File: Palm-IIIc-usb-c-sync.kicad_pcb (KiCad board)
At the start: 4 copper layers, 26 x 10 mm, 28 parts, among them J1 USB_C_Receptacle_USB2.0, J2 Conn_01x05, J3 Conn_01x05, U1 CP2102N-Axx-xQFN20, U2 TRSF3232E

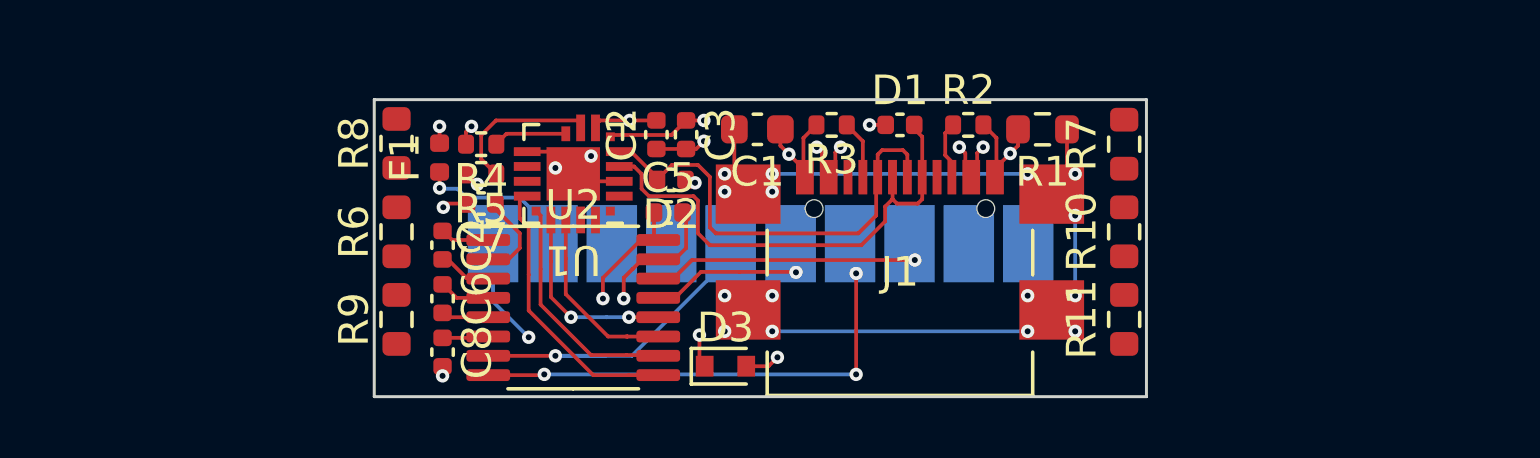
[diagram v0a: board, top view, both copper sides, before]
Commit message: Add manufacturing markings
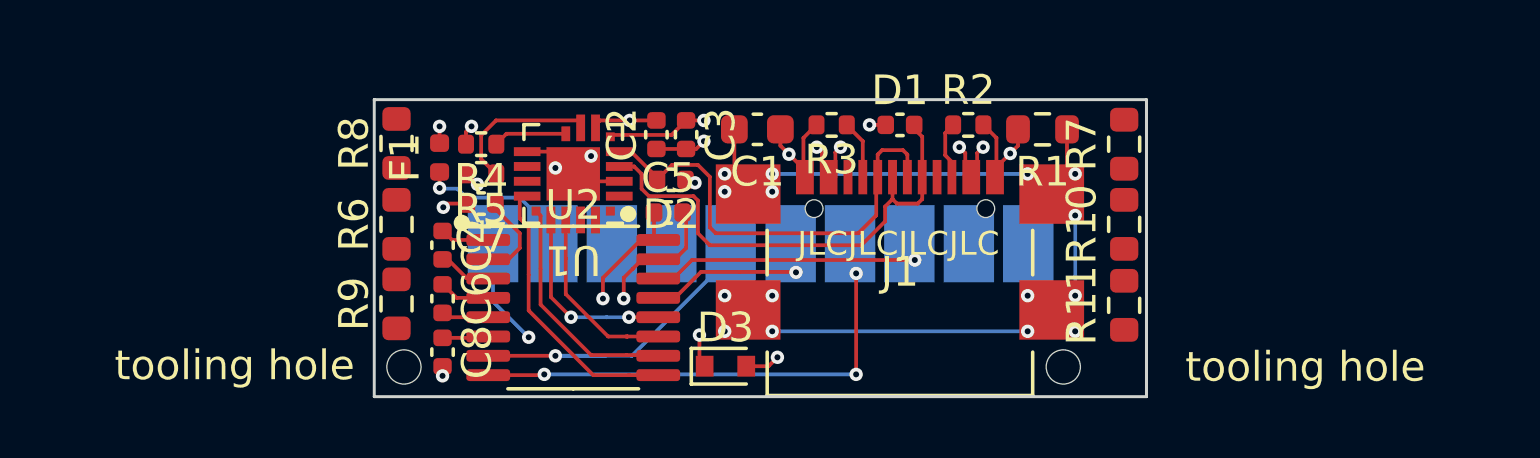
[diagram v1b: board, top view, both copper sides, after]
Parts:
- added H1: MountingHole, ToolingHole:ToolingHole_JLCSMT, F.Cu at (73.2, 59.0)
- added H2: MountingHole, ToolingHole:ToolingHole_JLCSMT, F.Cu at (51.0, 59.0)
- moved R9 0.52 mm to (50.8, 56.9)
- moved R11 0.48 mm to (75.2, 56.9)
- moved R10 0.25 mm to (75.2, 54.2)
- moved R6 0.25 mm to (50.8, 54.2)
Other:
- board text added: "JLCJLCJLCJLC"
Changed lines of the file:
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@@
 (kicad_pcb (version 20211014) (generator pcbnew)
   (general
-    (thickness 4.69)
+    (thickness 1.999999)
   )
   (paper "A4")
@@
       (layer "F.Mask" (type "Top Solder Mask") (thickness 0.01))
       (layer "F.Cu" (type "copper") (thickness 0.035))
-      (layer "dielectric 1" (type "core") (thickness 1.51) (material "FR4") (epsilon_r 4.5) (loss_tangent 0.02))
+      (layer "dielectric 1" (type "core") (thickness 0.613333) (material "FR4") (epsilon_r 4.5) (loss_tangent 0.02))
       (layer "In1.Cu" (type "copper") (thickness 0.035))
-      (layer "dielectric 2" (type "prepreg") (thickness 1.51) (material "FR4") (epsilon_r 4.5) (loss_tangent 0.02))
+      (layer "dielectric 2" (type "prepreg") (thickness 0.613333) (material "FR4") (epsilon_r 4.5) (loss_tangent 0.02))
       (layer "In2.Cu" (type "copper") (thickness 0.035))
-      (layer "dielectric 3" (type "core") (thickness 1.51) (material "FR4") (epsilon_r 4.5) (loss_tangent 0.02))
+      (layer "dielectric 3" (type "core") (thickness 0.613333) (material "FR4") (epsilon_r 4.5) (loss_tangent 0.02))
       (layer "B.Cu" (type "copper") (thickness 0.035))
       (layer "B.Mask" (type "Bottom Solder Mask") (thickness 0.01))
@@
   (net 48 "unconnected-(R11-Pad1)")
   (net 49 "unconnected-(R11-Pad2)")
+  (footprint "ToolingHole:ToolingHole_JLCSMT" (layer "F.Cu")
+    (at 51 59)
+    (property "Sheetfile" "Palm-IIIc-usb-c-sync.kicad_sch")
+    (property "Sheetname" "")
+    (property "exclude_from_bom" "")
+    (attr through_hole exclude_from_bom)
+    (fp_text reference "H2" (at 0 0.5) (layer "F.SilkS") hide
+      (effects (font (size 1 1) (thickness 0.15)))
+    )
+    (fp_text value "MountingHole" (at 0 -0.5) (layer "F.Fab")
+      (effects (font (size 1 1) (thickness 0.15)))
+    )
+    (fp_text user "tooling hole" (at -5.7 -0.05) (layer "F.SilkS")
+      (effects (font (size 1 1) (thickness 0.15)))
+    )
+    (pad "" np_thru_hole circle locked (at 0 0) (size 1.152 1.152) (drill 1.152) (layers *.Cu *.Mask))
+  )
   (footprint "Diode_SMD:D_SOD-523" (layer "F.Cu")
     (at 61.825 58.975)
@@
   )
   (footprint "Resistor_SMD:R_0603_1608Metric" (layer "F.Cu")
-    (at 50.75 57.4 90)
+    (at 50.75 56.875 90)
     (descr "Resistor SMD 0603 (1608 Metric), square (rectangular) end terminal, IPC_7351 nominal, (Body size source: IPC-SM-782 page 72, https://www.pcb-3d.com/wordpress/wp-content/uploads/ipc-sm-782a_amendment_1_and_2.pdf), generated with kicad-footprint-generator")
     (tags "resistor")
@@
   (footprint "Package_DFN_QFN_SiLabs:SilivonLabs_QFN-20-1EP_3x3mm_P0.5mm_missing_pads" (layer "F.Cu")
     (at 56.7 52.5 180)
+    (property "LCSC" "C969913")
     (property "Sheetfile" "Palm-IIIc-usb-c-sync.kicad_sch")
     (property "Sheetname" "")
@@
     )
   )
+  (footprint "ToolingHole:ToolingHole_JLCSMT" (layer "F.Cu")
+    (at 73.2 59)
+    (property "Sheetfile" "Palm-IIIc-usb-c-sync.kicad_sch")
+    (property "Sheetname" "")
+    (property "exclude_from_bom" "")
+    (attr through_hole exclude_from_bom)
+    (fp_text reference "H1" (at 0 0.5) (layer "F.SilkS") hide
+      (effects (font (size 1 1) (thickness 0.15)))
+    )
+    (fp_text value "MountingHole" (at 0 -0.5) (layer "F.Fab")
+      (effects (font (size 1 1) (thickness 0.15)))
+    )
+    (fp_text user "tooling hole" (at 8.15 0) (layer "F.SilkS")
+      (effects (font (size 1 1) (thickness 0.15)))
+    )
+    (pad "" np_thru_hole circle locked (at 0 0) (size 1.152 1.152) (drill 1.152) (layers *.Cu *.Mask))
+  )
   (footprint "Capacitor_SMD:C_0402_1005Metric" (layer "F.Cu")
     (at 67.7 50.85)
@@
     (descr "TSSOP, 16 Pin (JEDEC MO-153 Var AB https://www.jedec.org/document_search?search_api_views_fulltext=MO-153), generated with kicad-footprint-generator ipc_gullwing_generator.py")
     (tags "TSSOP SO")
+    (property "LCSC" "C2671080")
     (property "Sheetfile" "Palm-IIIc-usb-c-sync.kicad_sch")
     (property "Sheetname" "")
@@
   (footprint "Connector_SOFNG:MC-311S" (layer "F.Cu")
     (at 67.7 56.3)
+    (property "LCSC" "C2977718")
     (property "Sheetfile" "Palm-IIIc-usb-c-sync.kicad_sch")
     (property "Sheetname" "")
@@
   )
   (footprint "Resistor_SMD:R_0603_1608Metric" (layer "F.Cu")
-    (at 75.25 54.45 90)
+    (at 75.25 54.2 90)
     (descr "Resistor SMD 0603 (1608 Metric), square (rectangular) end terminal, IPC_7351 nominal, (Body size source: IPC-SM-782 page 72, https://www.pcb-3d.com/wordpress/wp-content/uploads/ipc-sm-782a_amendment_1_and_2.pdf), generated with kicad-footprint-generator")
     (tags "resistor")
@@
   )
   (footprint "Resistor_SMD:R_0603_1608Metric" (layer "F.Cu")
-    (at 75.25 57.4 90)
+    (at 75.25 56.925 90)
     (descr "Resistor SMD 0603 (1608 Metric), square (rectangular) end terminal, IPC_7351 nominal, (Body size source: IPC-SM-782 page 72, https://www.pcb-3d.com/wordpress/wp-content/uploads/ipc-sm-782a_amendment_1_and_2.pdf), generated with kicad-footprint-generator")
     (tags "resistor")
@@
   )
   (footprint "Resistor_SMD:R_0603_1608Metric" (layer "F.Cu")
-    (at 50.75 54.45 90)
+    (at 50.75 54.2 90)
     (descr "Resistor SMD 0603 (1608 Metric), square (rectangular) end terminal, IPC_7351 nominal, (Body size source: IPC-SM-782 page 72, https://www.pcb-3d.com/wordpress/wp-content/uploads/ipc-sm-782a_amendment_1_and_2.pdf), generated with kicad-footprint-generator")
     (tags "resistor")
@@
       (net 24 "/CTS") (pinfunction "Pin_5") (pintype "passive"))
   )
+  (gr_circle (center 52.95 54.15) (end 53.15 54.15) (layer "F.SilkS") (width 0.15) (fill solid))
+  (gr_circle (center 58.55 53.85) (end 58.75 53.85) (layer "F.SilkS") (width 0.15) (fill solid))
   (gr_rect (start 50 50) (end 76 60) (layer "Edge.Cuts") (width 0.1) (fill none))
   (gr_text "USB-C Palm Serial sync adapter\nRev 1.0   Tobias Schramm 2023" (at 75.8 51.8) (layer "B.SilkS")
     (effects (font (size 1 1) (thickness 0.15)) (justify left mirror))
   )
+  (gr_text "JLCJLCJLCJLC" (at 67.65 54.85) (layer "F.SilkS")
+    (effects (font (size 0.8 0.8) (thickness 0.15)))
+  )
   (segment (start 70.95 51.29) (end 70.95 52.575) (width 0.127) (layer "F.Cu") (net 9))
